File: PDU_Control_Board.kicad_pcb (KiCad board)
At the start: 4 copper layers, 170.4 x 233.5 mm, 220 parts, among them J1 Current_Sensor, J10 Precharge_2, J11 Shunt_2, J12 VIN_Enable, J13 1-776087-1, J14 Resistor, J15 GNDPWR, J16 VDC_OUT1_Relay, J17 VDC_OUT2_Rela, J2 Shunt_1, J20 VDC_IN, J21 VDC_OUT1, J22 VDC_OUT2, J3 SWD, J4 Precharge_1, J5 Precharge_2, J6 Shunt_2, J7 VIN_Enable, J8 Precharge_1, J9 Shunt_1, Q1 BSP75N, Q10 BC817, Q2 BSP75N, Q3 BSP75N, Q4 BSP75N, Q5 BSP75N, Q6 BC817, Q7 BC817, Q8 BC817, Q9 BC817, U1 LMV321, U2 APM32F405xG, U3 LMV321, U4 LMV321, U5 LMV321, U6 LMV321, Y2 X322516MOB4SI

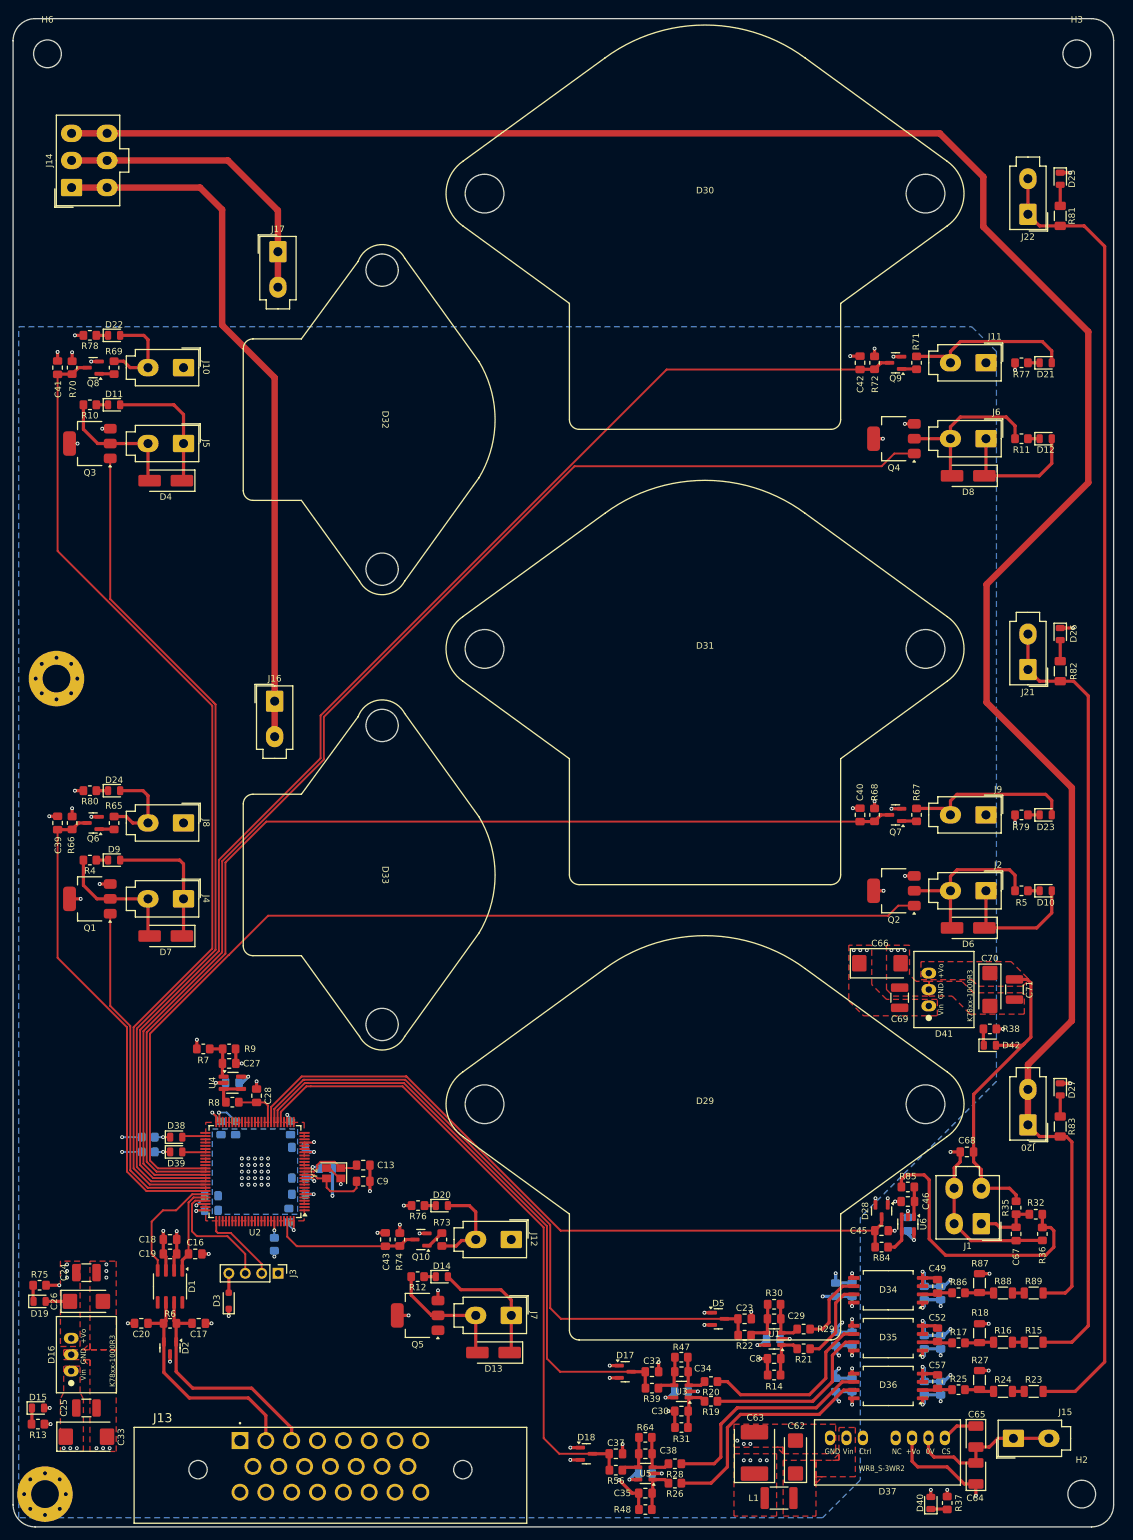
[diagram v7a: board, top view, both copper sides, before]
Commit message: VER1.0: подвинул крепежные отверстия
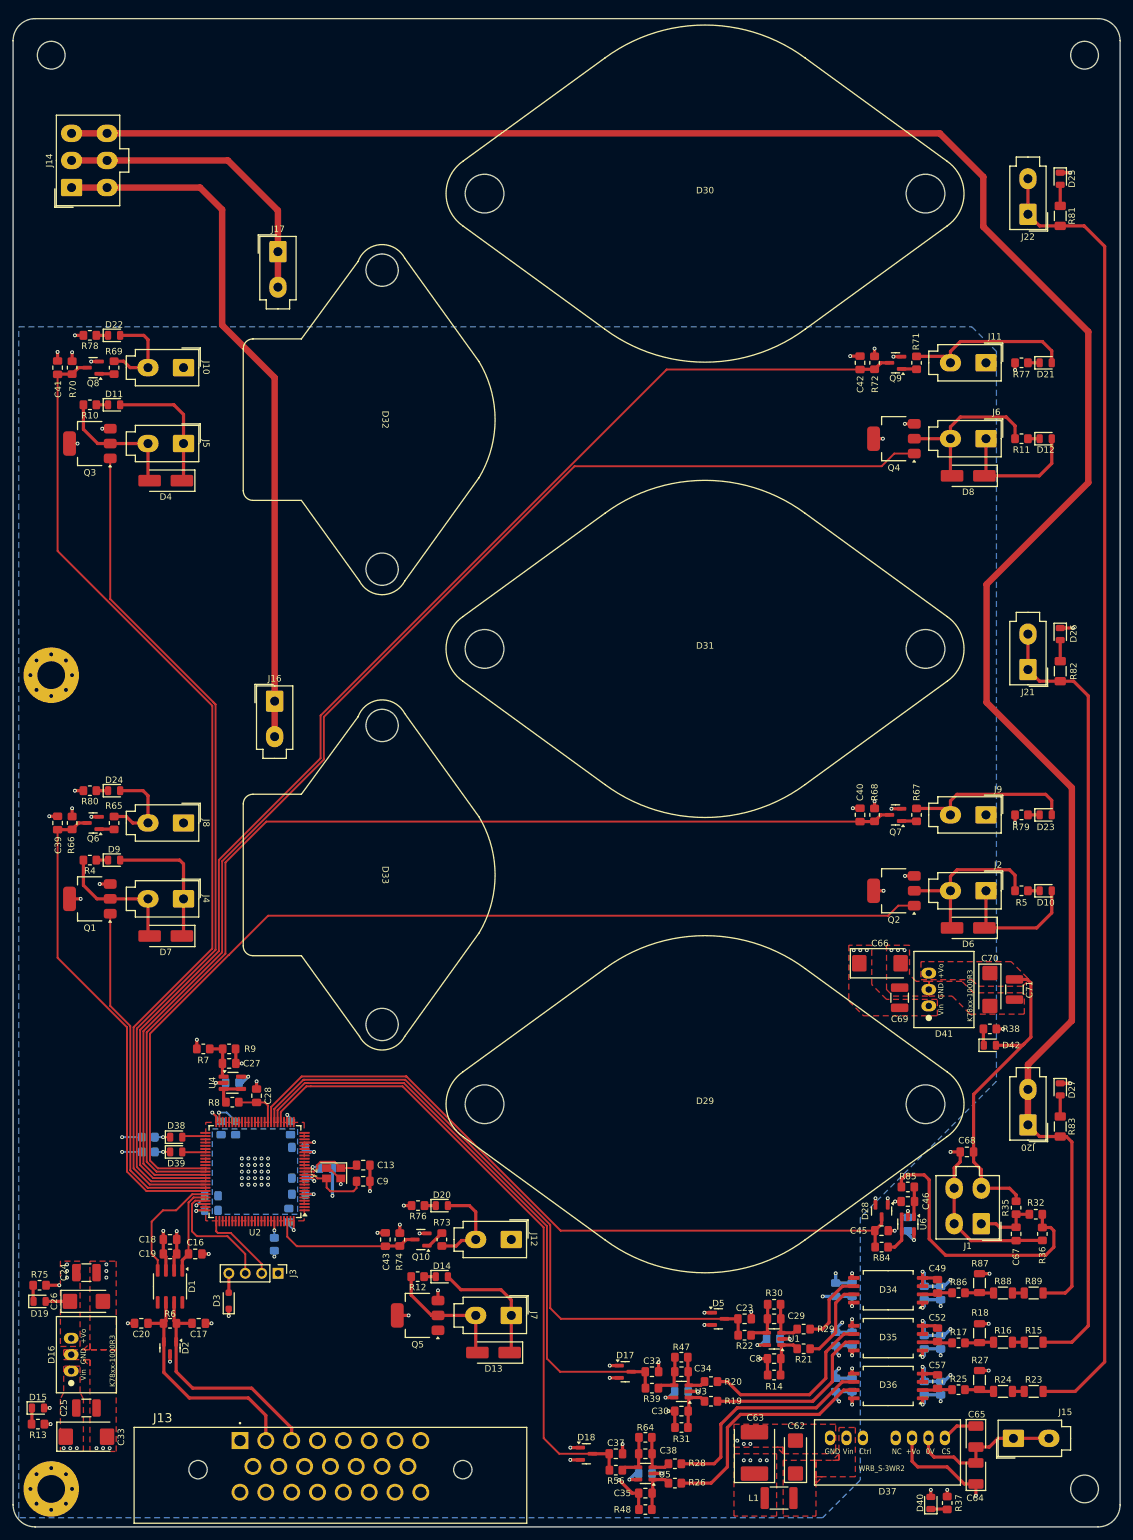
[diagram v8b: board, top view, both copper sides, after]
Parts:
- moved H4 1.26 mm to (146.0, 320.0)
- moved H3 1.22 mm to (306.0, 98.0)
- moved H1 0.97 mm to (146.0, 194.0)
- moved H2 0.91 mm to (306.0, 320.0)
- moved H6 0.62 mm to (146.0, 98.0)
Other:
- board size 170.4 x 233.5 mm -> 171.4 x 233.5 mm
